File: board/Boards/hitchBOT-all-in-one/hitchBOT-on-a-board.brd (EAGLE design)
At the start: 100 x 55 mm, 40 parts, among them J1 22-27-2021-02, J2 22-27-2021-02, J3 22-27-2021-02, Q1 SPD30P06PTO252, Q2 SPD30P06PTO252, Q3 SPD30P06PTO252

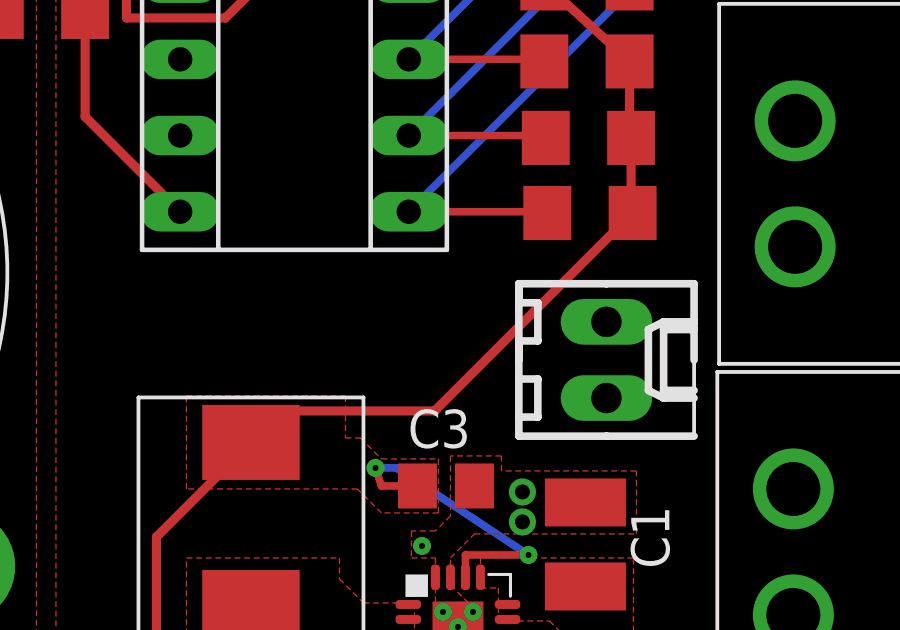
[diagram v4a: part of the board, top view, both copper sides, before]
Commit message: added missed airwires from past ripup
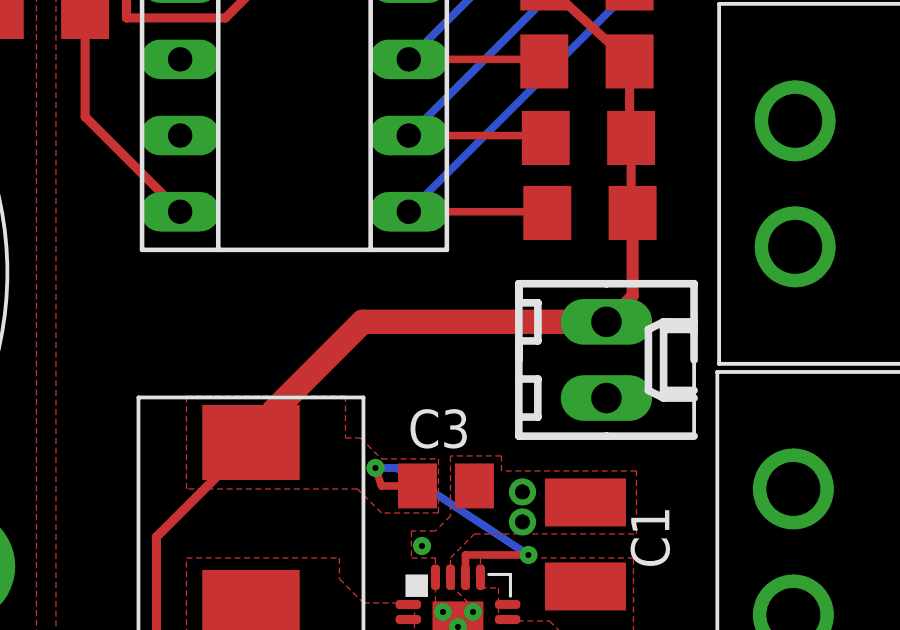
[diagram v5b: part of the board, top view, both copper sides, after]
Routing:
- net N$15: track 71.1 -> 72.8 mm
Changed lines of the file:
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@@
 <wire x1="59" y1="29.2" x2="59" y2="33.8" width="0.3048" layer="1"/>
 <wire x1="59" y1="33.8" x2="62.15" y2="36.95" width="0.3048" layer="1"/>
-<wire x1="74.872" y1="44.6" x2="68.272" y2="38" width="0.3048" layer="1"/>
-<wire x1="68.272" y1="38" x2="62.9" y2="38" width="0.3048" layer="1"/>
 <wire x1="62.9" y1="38" x2="62.15" y2="37.25" width="0.3048" layer="1"/>
 <wire x1="62.15" y1="37.25" x2="62.15" y2="36.95" width="0.3048" layer="1"/>
@@
 <wire x1="58" y1="51.1" x2="58" y2="53.3" width="0.3048" layer="1"/>
 <wire x1="58" y1="53.3" x2="56.95" y2="53.3" width="0.3048" layer="1"/>
-<wire x1="74.872" y1="44.6" x2="74" y2="40.97" width="0" layer="19" extent="1-1"/>
+<wire x1="74" y1="40.97" x2="65.87" y2="40.97" width="0.8128" layer="1"/>
+<wire x1="65.87" y1="40.97" x2="62.9" y2="38" width="0.8128" layer="1"/>
+<wire x1="74" y1="40.97" x2="74.872" y2="41.842" width="0.4064" layer="1"/>
+<wire x1="74.872" y1="41.842" x2="74.872" y2="44.6" width="0.4064" layer="1"/>
 </signal>
 <signal name="N$16">

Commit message: added labels, board considered finalized
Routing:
- net GND: track 27.3 -> 29.3 mm, vias 11 -> 27
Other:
- board text added: "12VB"
- board text added: "12VF"
- board text added: "5VB"
- board text added: "AUX IN"
- board text added: "AUX OUT"
- board text added: "HEAD OUT"
- board text added: "LAPTOP IN"
- board text added: "OPENUPS IN"
- board text added: "OPENUPS OUT"
- board text added: "SOLAR IN"
- board text added: "TABLET OUT"
- board text added: "UNSWITCHED 12V"
- board text added: "hitchBOT-all-in-one Power Shield Colin Gagich June 2016"
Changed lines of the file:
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@@
 <setting verticaltext="up"/>
 </settings>
-<grid distance="0.1" unitdist="mm" unit="mm" style="lines" multiple="1" display="no" altdistance="0.1" altunitdist="mm" altunit="mm"/>
+<grid distance="0.25" unitdist="mm" unit="mm" style="lines" multiple="1" display="no" altdistance="0.1" altunitdist="mm" altunit="mm"/>
 <layers>
 <layer number="1" name="Top" color="4" fill="1" visible="yes" active="yes"/>
@@
 <hole x="98" y="53" drill="2"/>
 <hole x="98" y="2" drill="2"/>
+<text x="65.5" y="39.75" size="1.778" layer="21">5VB</text>
+<text x="51.75" y="28.25" size="1.778" layer="21">12VB</text>
+<text x="3.75" y="2.5" size="1.778" layer="21">12VF</text>
+<text x="47.5" y="37.25" size="1.778" layer="22" rot="MR0">hitchBOT-all-in-one
+Power Shield
+Colin Gagich
+June 2016</text>
+<text x="3" y="40.25" size="1.016" layer="22" rot="MR270">OPENUPS OUT</text>
+<text x="45.75" y="2.75" size="1.016" layer="22" rot="MR180">LAPTOP IN</text>
+<text x="33" y="2.75" size="1.016" layer="22" rot="MR180">SOLAR IN</text>
+<text x="22.25" y="2.75" size="1.016" layer="22" rot="MR180">AUX IN</text>
+<text x="97.25" y="41" size="1.016" layer="22" rot="MR90">OPENUPS IN</text>
+<text x="98.5" y="38.25" size="1.016" layer="22" rot="MR270">UNSWITCHED
+12V</text>
+<text x="85.75" y="2.75" size="1.016" layer="22" rot="MR180">TABLET OUT</text>
+<text x="73" y="2.75" size="1.016" layer="22" rot="MR180">HEAD OUT</text>
+<text x="60" y="2.75" size="1.016" layer="22" rot="MR180">AUX OUT</text>
 </plain>
 <attributes>
@@
 <wire x1="14.33560625" y1="39.88439375" x2="14.41" y2="39.704790625" width="1.016" layer="1" curve="-44.999295"/>
 <wire x1="14.41" y1="39.704790625" x2="14.41" y2="37.46" width="1.016" layer="1"/>
-<wire x1="23.9" y1="43.79" x2="20.44439375" y2="40.33439375" width="1.016" layer="1"/>
-<wire x1="20.44439375" y1="40.33439375" x2="20.264790625" y2="40.26" width="1.016" layer="1" curve="-44.999295"/>
-<wire x1="20.264790625" y1="40.26" x2="13.96" y2="40.26" width="1.016" layer="1"/>
+<wire x1="23.9" y1="43.79" x2="18.69439375" y2="40.33439375" width="1.016" layer="1"/>
+<wire x1="18.69439375" y1="40.33439375" x2="18.264790625" y2="40.26" width="1.016" layer="1" curve="-44.999295"/>
+<wire x1="18.264790625" y1="40.26" x2="13.96" y2="40.26" width="1.016" layer="1"/>
 <contactref element="R7" pad="1"/>
 <contactref element="J2" pad="1"/>
@@
 <wire x1="56.622" y1="51.3" x2="56.622" y2="47.808" width="0.3048" layer="1"/>
 <wire x1="56.622" y1="47.808" x2="59.79" y2="44.64" width="0.3048" layer="1"/>
-<wire x1="13.58" y1="14.63" x2="13.54" y2="20.37" width="0" layer="19" extent="1-1"/>
-<wire x1="22.27" y1="14.41" x2="13.58" y2="14.63" width="0" layer="19" extent="1-1"/>
-<wire x1="4.71" y1="20.37" x2="13.54" y2="20.37" width="0" layer="19" extent="1-1"/>
-<wire x1="4.77" y1="14.63" x2="4.71" y2="20.37" width="0" layer="19" extent="1-1"/>
+<via x="4.25" y="15.75" extent="1-16" drill="0.6"/>
+<via x="5.5" y="15.75" extent="1-16" drill="0.6"/>
+<via x="5.5" y="14.5" extent="1-16" drill="0.6"/>
+<via x="4.25" y="14.5" extent="1-16" drill="0.6"/>
+<via x="13" y="15.75" extent="1-16" drill="0.6"/>
+<via x="14.25" y="15.75" extent="1-16" drill="0.6"/>
+<via x="14.25" y="14.5" extent="1-16" drill="0.6"/>
+<via x="13" y="14.5" extent="1-16" drill="0.6"/>
+<via x="13" y="19.25" extent="1-16" drill="0.6"/>
+<via x="14.25" y="19.25" extent="1-16" drill="0.6"/>
+<via x="14.25" y="20.5" extent="1-16" drill="0.6"/>
+<via x="13" y="20.5" extent="1-16" drill="0.6"/>
+<via x="5.25" y="19.25" extent="1-16" drill="0.6"/>
+<via x="4" y="19.25" extent="1-16" drill="0.6"/>
+<via x="4" y="20.5" extent="1-16" drill="0.6"/>
+<via x="5.25" y="20.5" extent="1-16" drill="0.6"/>
+<wire x1="5.25" y1="20.5" x2="5.12" y2="20.37" width="0.4064" layer="1"/>
+<wire x1="5.12" y1="20.37" x2="4.71" y2="20.37" width="0.4064" layer="1"/>
+<wire x1="13" y1="20.5" x2="13.13" y2="20.37" width="0.4064" layer="1"/>
+<wire x1="13.13" y1="20.37" x2="13.54" y2="20.37" width="0.4064" layer="1"/>
+<wire x1="13.58" y1="14.63" x2="13.45" y2="14.5" width="0.4064" layer="1"/>
+<wire x1="13.45" y1="14.5" x2="13" y2="14.5" width="0.4064" layer="1"/>
+<wire x1="4.25" y1="14.5" x2="4.38" y2="14.63" width="0.4064" layer="1"/>
+<wire x1="4.38" y1="14.63" x2="4.77" y2="14.63" width="0.4064" layer="1"/>
 </signal>
 <signal name="N$2">
@@
 <wire x1="62.15" y1="37.25" x2="62.15" y2="36.95" width="0.3048" layer="1"/>
 <wire x1="74.872" y1="44.6" x2="74.822" y2="44.65" width="0.3048" layer="1"/>
-<wire x1="74.822" y1="44.65" x2="74.822" y2="47.1" width="0.3048" layer="1"/>
+<wire x1="74.822" y1="44.65" x2="74.822" y2="47.1" width="0.4064" layer="1"/>
 <wire x1="74.822" y1="47.1" x2="74.772" y2="47.15" width="0.3048" layer="1"/>
 <wire x1="74.772" y1="47.15" x2="74.772" y2="49.65" width="0.3048" layer="1"/>
@@
 </board>
 </drawing>
+<compatibility>
+<note version="6.3" minversion="6.2.2" severity="warning">
+Since Version 6.2.2 text objects can contain more than one line,
+which will not be processed correctly with this version.
+</note>
+</compatibility>
 </eagle>
